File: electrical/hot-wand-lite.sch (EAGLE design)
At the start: 83 parts, among them IC1 12V R-78K12-2.0, IC2 AMS1117-5.0, Q1 NCHAN, Q2 SIS862ADN-T1-GE3, Q3 DMTH64M2LPDWQ-13, Q4 2N7002K, Q5 SIS862ADN-T1-GE3, U1 SEEED-XIAO-SAMD21-TH-LOCKING, U2 1EDN8511BXUSA1, U3 LM74700QDBVTQ1, U4 AP53781

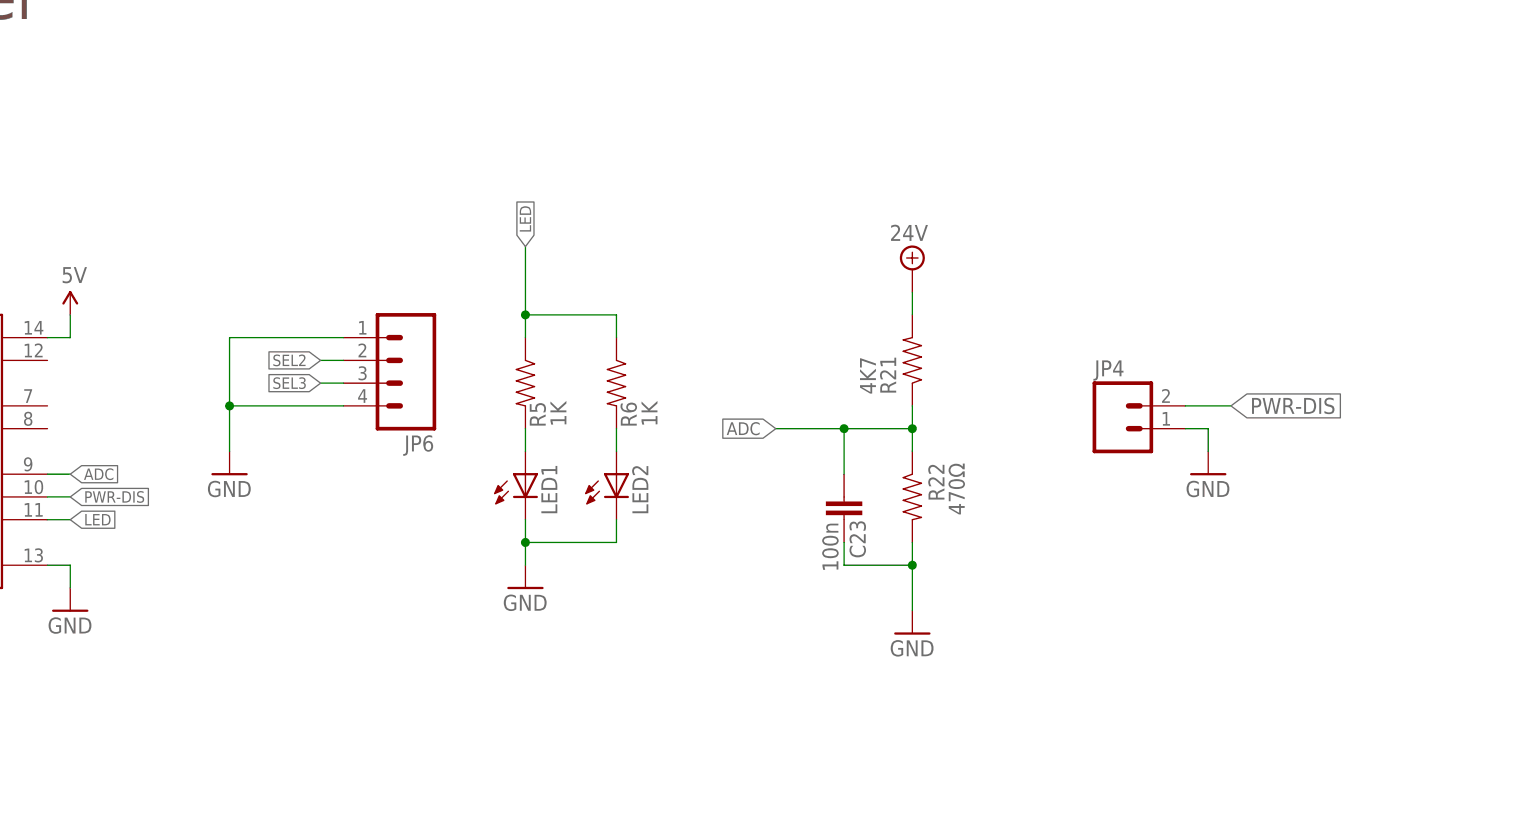
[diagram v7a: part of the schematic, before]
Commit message: lite pcb, added esd tvs diodes
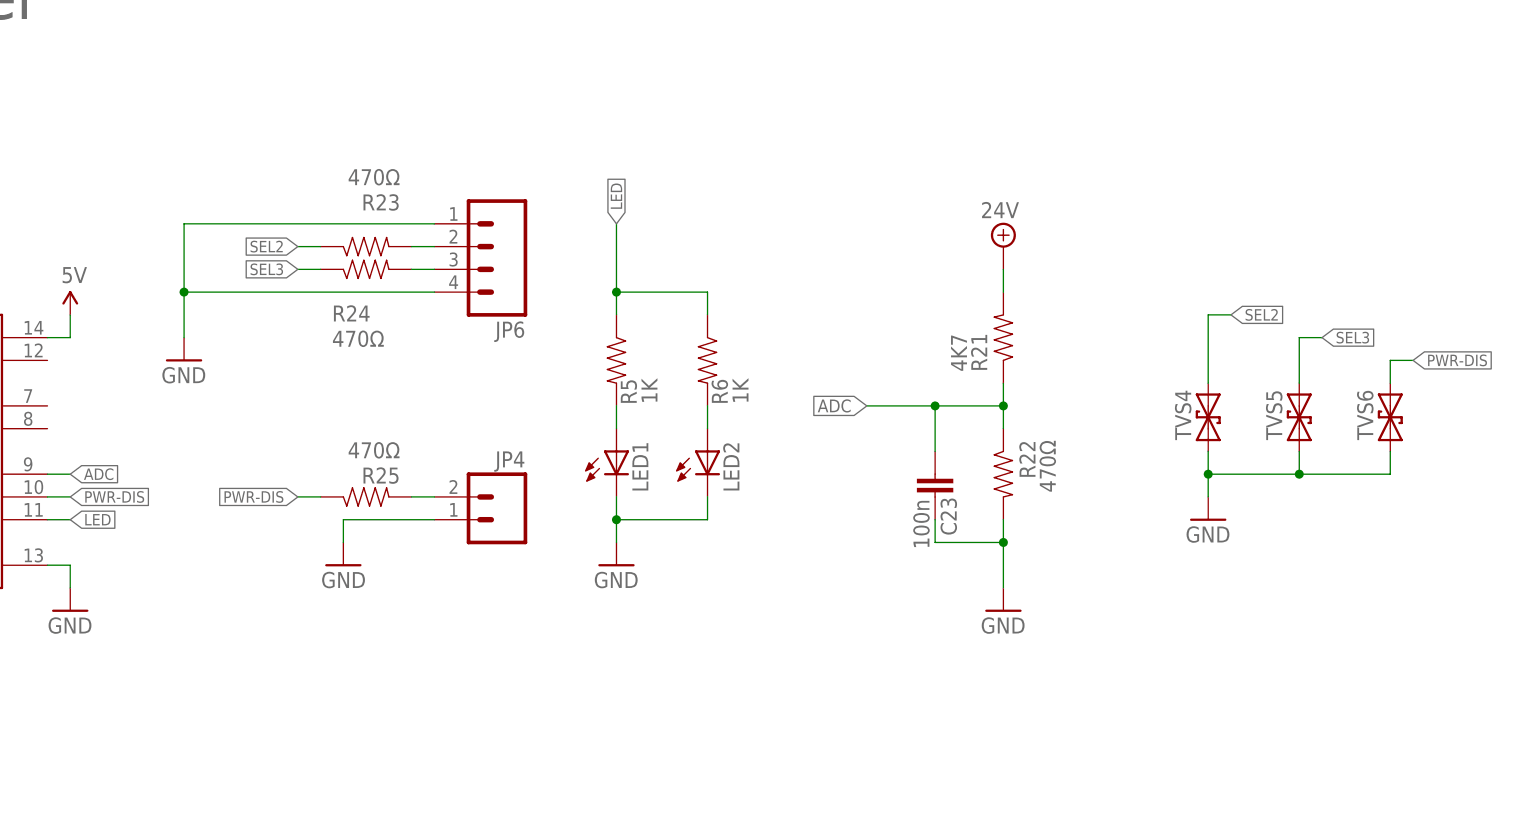
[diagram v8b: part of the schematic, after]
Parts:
- added R23, R24, R25: 470Ω, hot-wand:RESISTOR0603-RES
- added TVS4, TVS5, TVS6: TVSSOD323-R, hot-wand:TVSSOD323-R
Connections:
- new net N$17: JP6.2, R23.2
- new net N$18: JP6.3, R24.2
- new net N$21: JP4.2, R25.2
- net GND: now also TVS4.1, TVS5.1, TVS6.1
- net PWR-DIS: now also R25.1, TVS6.2; no longer JP4.2
- net SEL2: now also R23.1, TVS4.2; no longer JP6.2
- net SEL3: now also R24.1, TVS5.2; no longer JP6.3
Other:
- moved on the sheet: C23, JP4, JP6, LED1, LED2, R21, R22, R5, R6
